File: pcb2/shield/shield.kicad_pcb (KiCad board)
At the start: 2 copper layers, 17 parts, among them IC1 AM26C31CNSR, IC2 AM26C31CNSR, P1 ARD_NW, P10 BUS5, P11 BUS6, P12 BUS7, P13 BUS8, P2 ARD_SW, P3 ARD_NE, P4 ARD_SE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

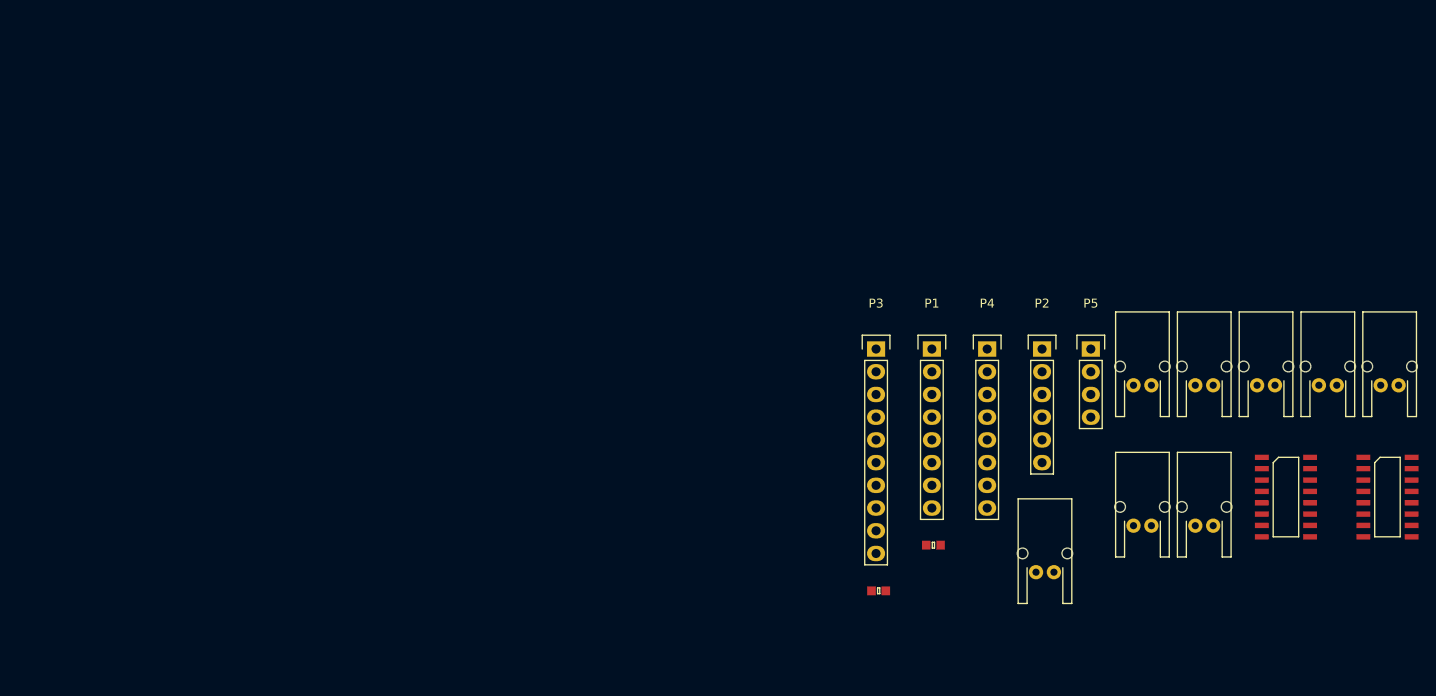
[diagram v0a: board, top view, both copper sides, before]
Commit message: Proof of concept route of shield
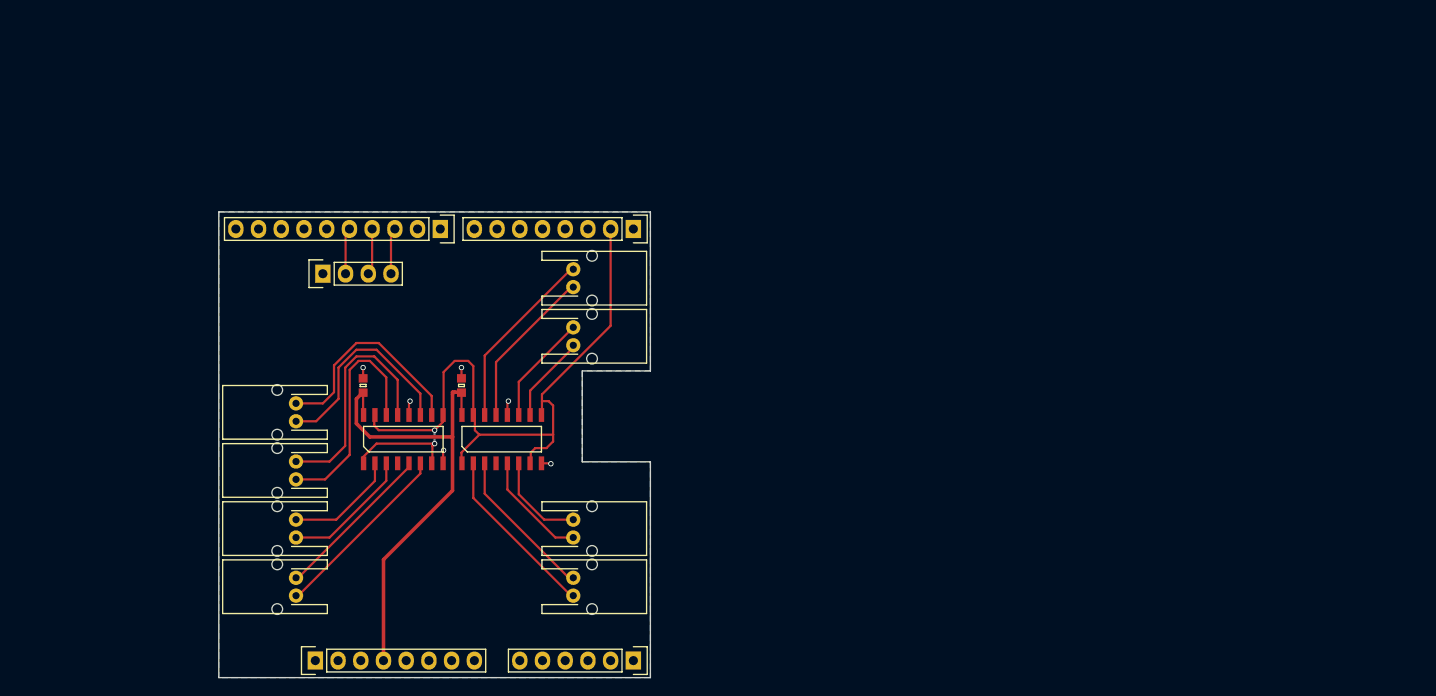
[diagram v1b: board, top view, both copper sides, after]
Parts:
- moved P6 123.3 mm to (71.5, 97.0), turned to 90 degrees
- moved P8 115.4 mm to (71.5, 84.0), turned to 90 degrees
- moved IC1 110.2 mm to (83.5, 87.0), turned to 90 degrees
- moved P9 101.7 mm to (71.5, 90.5), turned to 90 degrees
- moved P7 97.3 mm to (71.5, 103.5), turned to 90 degrees
- moved IC2 87.9 mm to (94.5, 87.0), turned to 90 degrees
- moved P5 86.3 mm to (74.5, 68.5), turned to 90 degrees
- moved P10 80.7 mm to (102.5, 103.5), turned to 270 degrees
- moved P1 77.2 mm to (73.7, 111.8), turned to 90 degrees
- moved P13 71.6 mm to (102.5, 69.0), turned to 270 degrees
- moved C2 66.2 mm to (79.0, 81.0), turned to 90 degrees
- moved P11 63.6 mm to (102.5, 97.0), turned to 270 degrees
- moved P12 59.0 mm to (102.5, 75.5), turned to 270 degrees
- moved P2 57.5 mm to (109.2, 111.8), turned to 270 degrees
- moved C1 52.0 mm to (90.0, 81.0), turned to 90 degrees
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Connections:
- IC1 pad 12: (no net) -> GND
- IC1 pad 4: +5V -> (no net)
- IC2 pad 12: (no net) -> GND
- IC2 pad 4: +5V -> (no net)
- P3 pad 3: (no net) -> /SHIFT_DATA
- P3 pad 4: (no net) -> /SHIFT_SRCK
- P3 pad 5: (no net) -> /SHIFT_RCK
- P5 pad 2: (no net) -> /SHIFT_RCK
- P5 pad 3: (no net) -> /SHIFT_SRCK
- P5 pad 4: (no net) -> /SHIFT_DATA
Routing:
- net /TX: track 0.00 -> 87.4 mm, vias 0 -> 2
- net +5V: track 0.00 -> 54.5 mm
- net Net-(IC1-Pad13): track 0.00 -> 26.4 mm
- net Net-(IC1-Pad14): track 0.00 -> 26.1 mm
- net Net-(IC1-Pad10): track 0.00 -> 24.3 mm
- net Net-(IC1-Pad11): track 0.00 -> 23.7 mm
- net Net-(IC1-Pad6): track 0.00 -> 21.1 mm
- net Net-(IC2-Pad14): track 0.00 -> 20.9 mm
- net Net-(IC2-Pad2): track 0.00 -> 19.6 mm
- net Net-(IC1-Pad5): track 0.00 -> 18.2 mm
- net Net-(IC2-Pad13): track 0.00 -> 18.0 mm
- net Net-(IC2-Pad3): track 0.00 -> 17.4 mm
- net Net-(IC1-Pad3): track 0.00 -> 14.7 mm
- net Net-(IC1-Pad2): track 0.00 -> 12.6 mm
- net Net-(IC2-Pad5): track 0.00 -> 12.5 mm
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- added copper zone on B.Cu, net GND
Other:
- board outline added: 48.3 x 52.1 mm

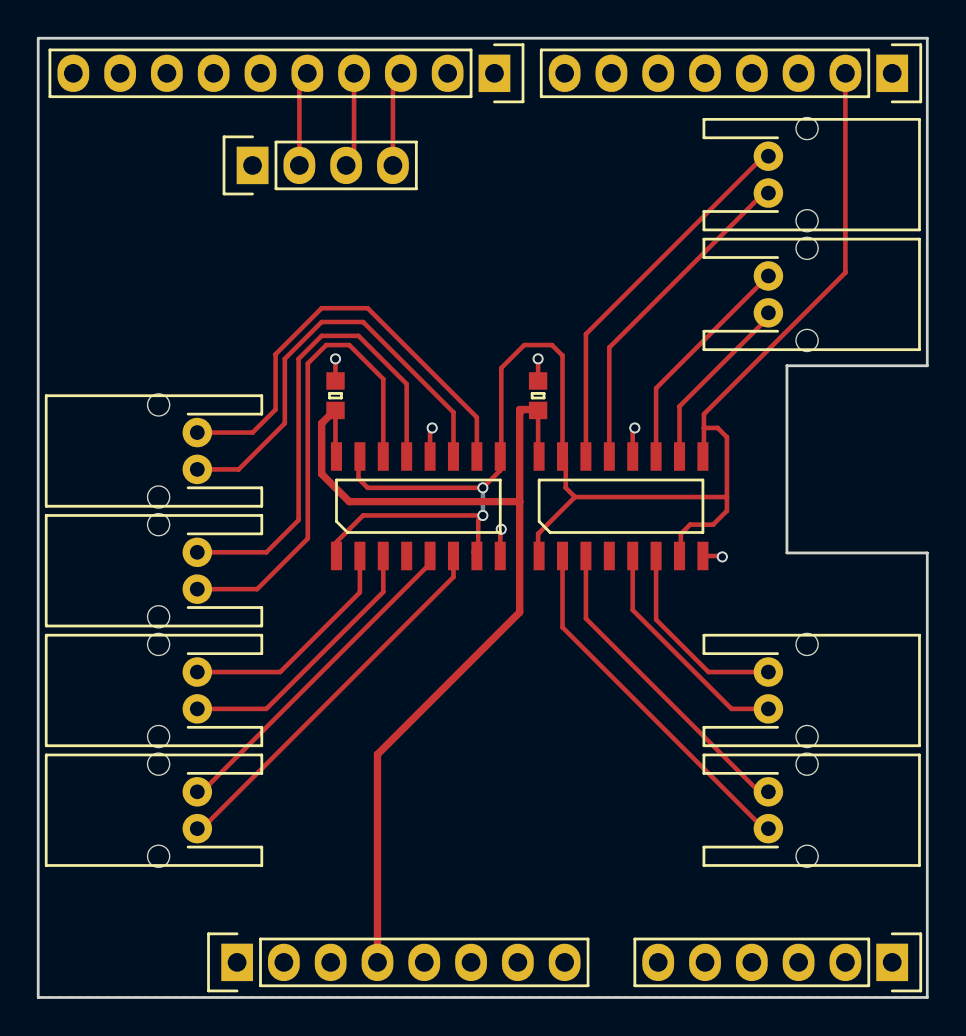
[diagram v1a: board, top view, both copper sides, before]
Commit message: Cleared up routing, added+stitched top gnd plane
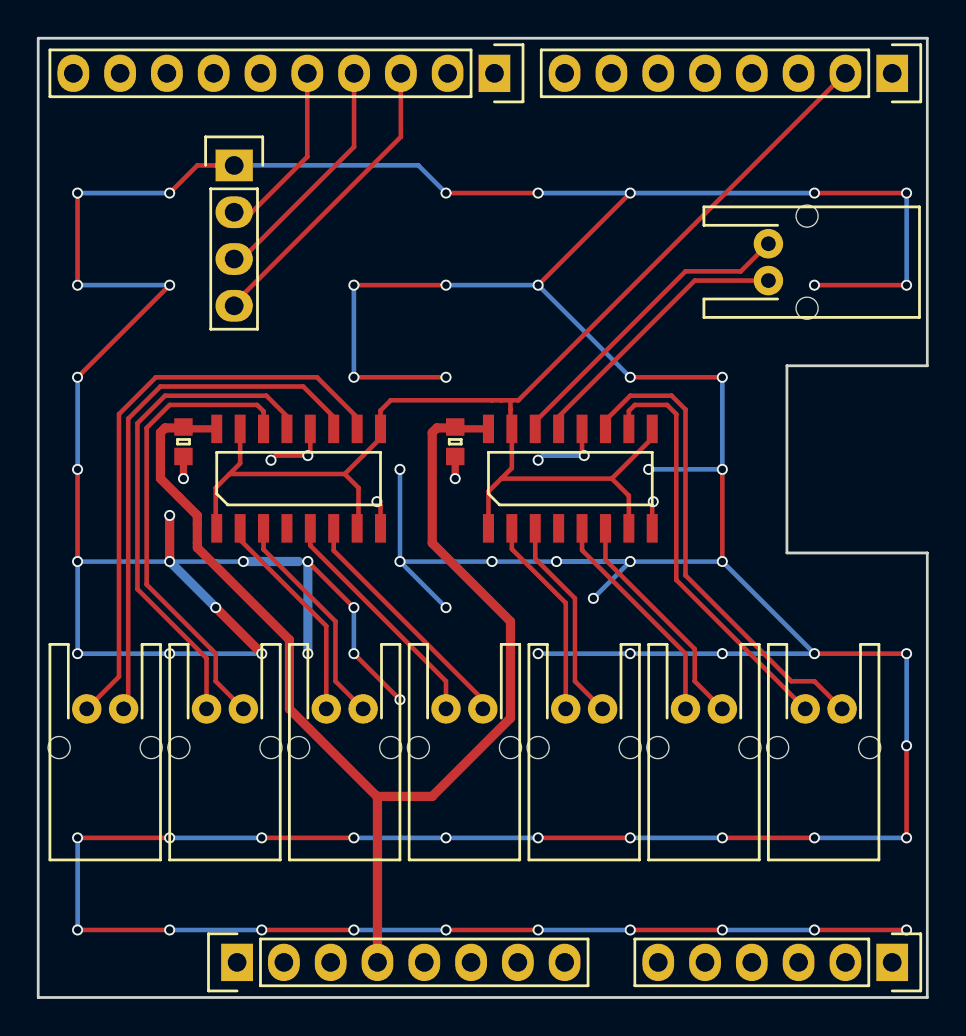
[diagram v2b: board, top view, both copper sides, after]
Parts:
- moved P12 22.7 mm to (105.5, 98.0), turned to 180 degrees
- moved P7 15.5 mm to (86.0, 98.0), turned to 180 degrees
- moved P8 14.9 mm to (66.5, 98.0), turned to 180 degrees
- moved P10 11.4 mm to (92.5, 98.0), turned to 180 degrees
- moved C2 8.62 mm to (70.8, 83.5), turned to 270 degrees
- moved P6 8.06 mm to (79.5, 98.0), turned to 180 degrees
- moved P9 7.65 mm to (73.0, 98.0), turned to 180 degrees
- moved IC1 6.67 mm to (77.0, 85.5)
- moved C1 5.15 mm to (85.5, 83.5), turned to 270 degrees
- moved P13 4.75 mm to (102.5, 73.8)
- moved P11 3.64 mm to (99.0, 98.0), turned to 180 degrees
- moved IC2 3.13 mm to (91.8, 85.5)
- moved P5 1.00 mm to (73.5, 68.5), turned to 0 degrees
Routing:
- net GND: track 8.14 -> 369.1 mm, vias 6 -> 77
- net Net-(IC2-Pad11): track 12.3 -> 26.2 mm
- net /TX: track 87.4 -> 73.6 mm, vias 2 -> 0
- net Net-(IC2-Pad10): track 9.80 -> 22.8 mm
- net +5V: track 54.5 -> 66.5 mm
- net /SHIFT_DATA: track 5.16 -> 16.4 mm
- net Net-(IC2-Pad2): track 19.6 -> 11.0 mm
- net Net-(IC1-Pad6): track 21.1 -> 13.2 mm
- net /SHIFT_SRCK: track 5.29 -> 13.1 mm
- net Net-(IC1-Pad10): track 24.3 -> 32.0 mm
- net Net-(IC2-Pad3): track 17.4 -> 11.3 mm
- net Net-(IC1-Pad11): track 23.7 -> 29.1 mm
- net Net-(IC1-Pad5): track 18.2 -> 12.9 mm
- net /SHIFT_RCK: track 5.19 -> 9.75 mm
- net Net-(IC2-Pad14): track 20.9 -> 17.0 mm
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- added copper zone on F.Cu, net GND

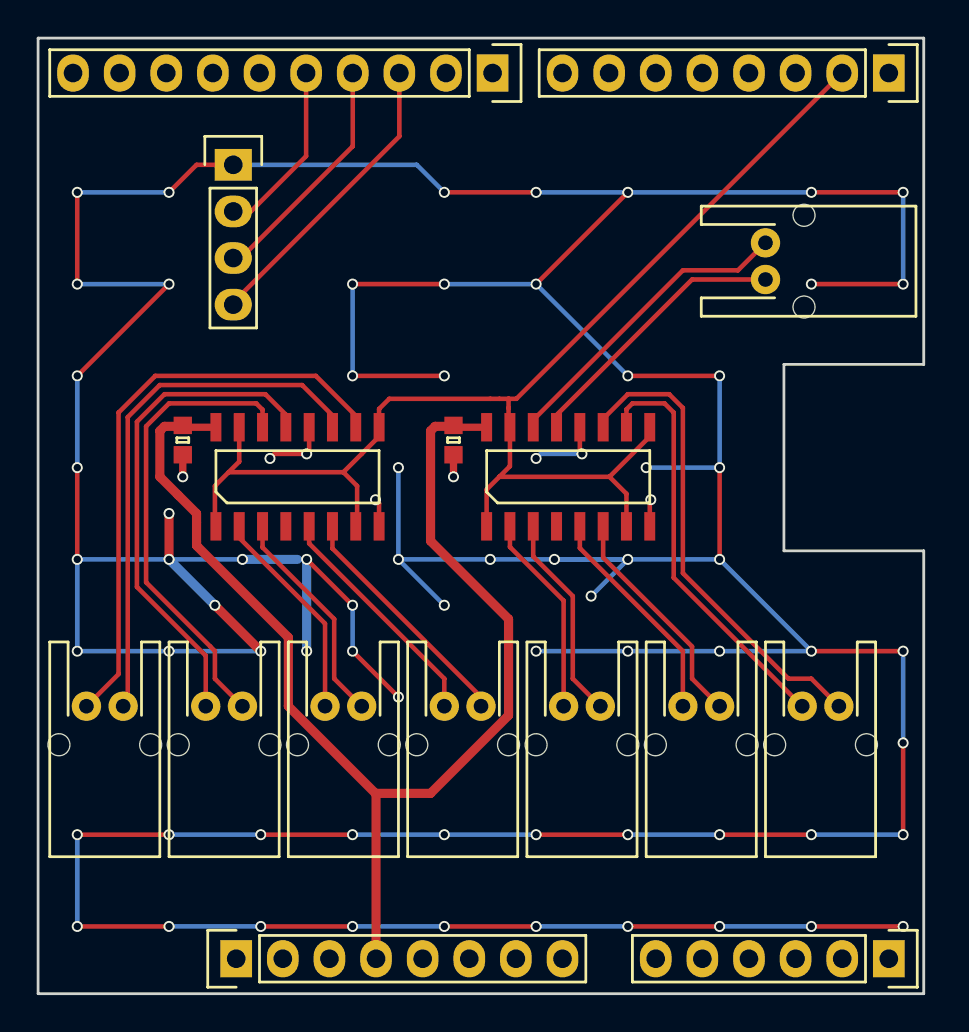
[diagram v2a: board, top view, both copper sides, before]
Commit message: Moved JST-PAs inward, silk
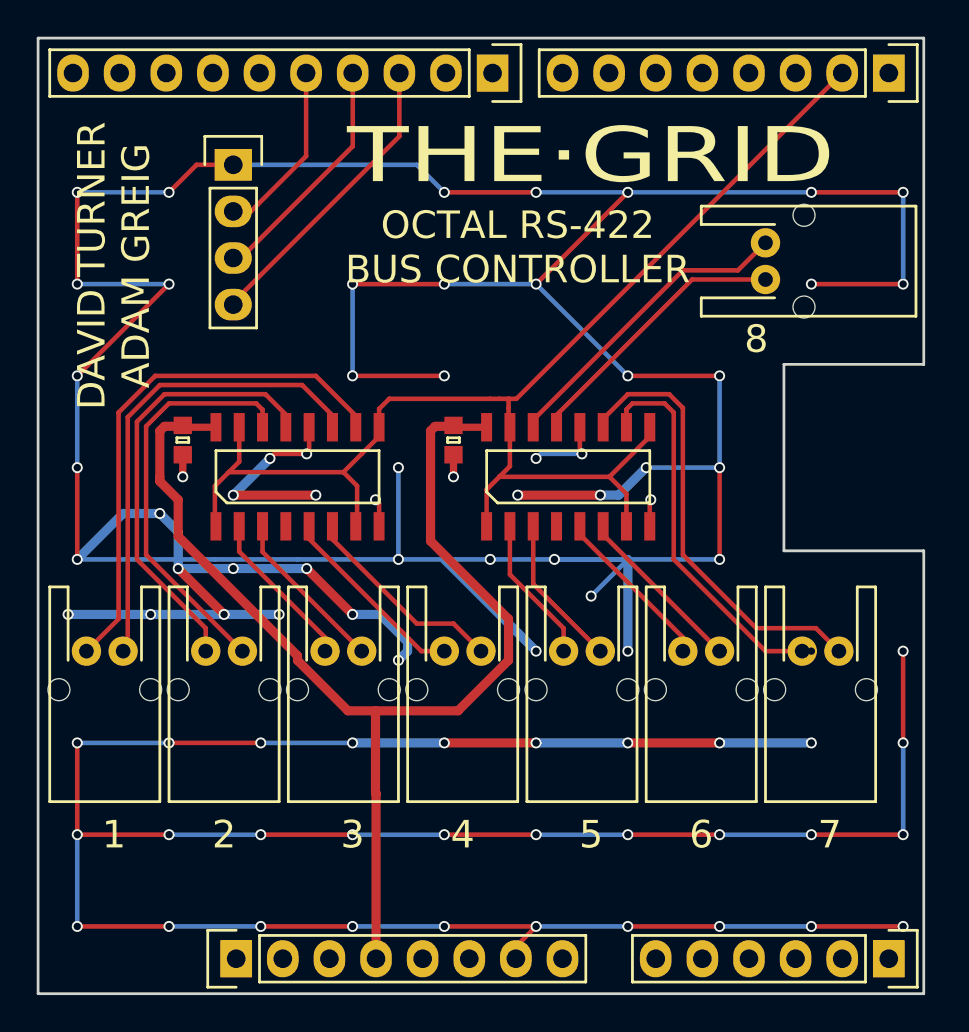
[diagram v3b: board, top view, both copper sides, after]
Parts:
- moved P10 3.00 mm to (92.5, 95.0)
- moved P11 3.00 mm to (99.0, 95.0)
- moved P12 3.00 mm to (105.5, 95.0)
- moved P6 3.00 mm to (79.5, 95.0)
- moved P7 3.00 mm to (86.0, 95.0)
- moved P8 3.00 mm to (66.5, 95.0)
- moved P9 3.00 mm to (73.0, 95.0)
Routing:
- net GND: track 369.1 -> 415.0 mm, vias 77 -> 84
- net Net-(IC1-Pad11): track 29.1 -> 26.1 mm
- net Net-(IC1-Pad10): track 32.0 -> 29.0 mm
- net Net-(IC2-Pad6): track 12.4 -> 9.43 mm, vias 0 -> 1
- net Net-(IC2-Pad5): track 12.1 -> 9.13 mm
- net Net-(IC2-Pad2): track 11.0 -> 8.01 mm
- net Net-(IC1-Pad3): track 12.0 -> 9.04 mm
- net Net-(IC1-Pad13): track 26.9 -> 23.9 mm
- net Net-(IC2-Pad3): track 11.3 -> 8.31 mm
- net Net-(IC1-Pad14): track 25.4 -> 22.4 mm
- net +5V: track 66.5 -> 63.8 mm
- net Net-(IC1-Pad2): track 11.7 -> 9.36 mm
- net Net-(IC1-Pad5): track 12.9 -> 10.6 mm
- net Net-(IC1-Pad6): track 13.2 -> 11.3 mm
- net Net-(IC2-Pad11): track 26.2 -> 24.3 mm
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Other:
- board text added: "-DATA"
- board text added: "-RCK"
- board text added: "-SRCK"
- board text added: "-TX"
- board text added: "1"
- board text added: "1 GND 2 RCK 3 SRCK 4 DATA"
- board text added: "2"
- board text added: "2016-03-28"
- board text added: "3"
- board text added: "4"
- board text added: "5"
- board text added: "6"
- board text added: "7"
- board text added: "8"
- board text added: "DAVID TURNER ADAM GREIG"
- board text added: "OCTAL RS-422 BUS CONTROLLER"
- board text added: "Revision 1"
- board text added: "THE·GRID"

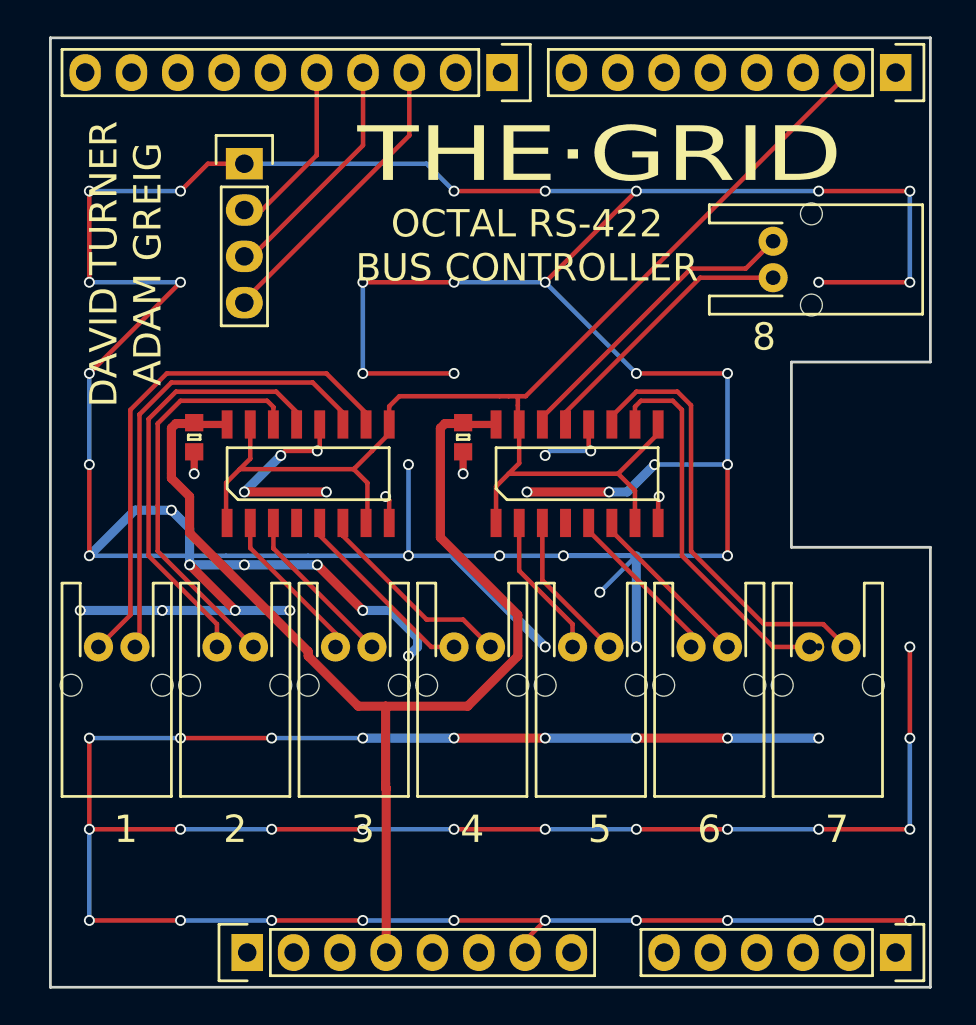
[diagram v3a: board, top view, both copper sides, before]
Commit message: Shrunk shield board outline to fit 5x5
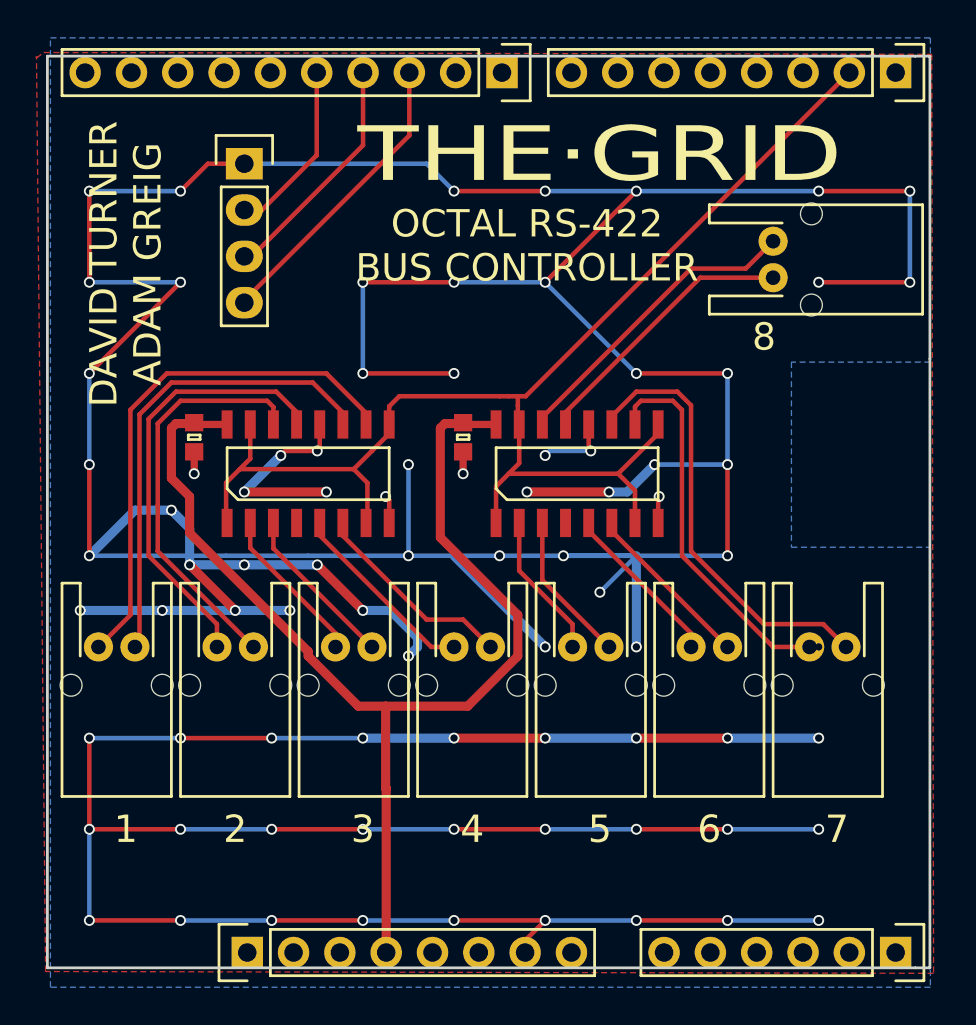
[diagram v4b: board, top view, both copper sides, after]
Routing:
- net GND: track 415.0 -> 395.0 mm, vias 84 -> 80
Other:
- board size 48.3 x 52.1 mm -> 48.4 x 50 mm
